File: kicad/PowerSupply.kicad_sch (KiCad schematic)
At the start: 10 parts, among them U3 LM2611xMF

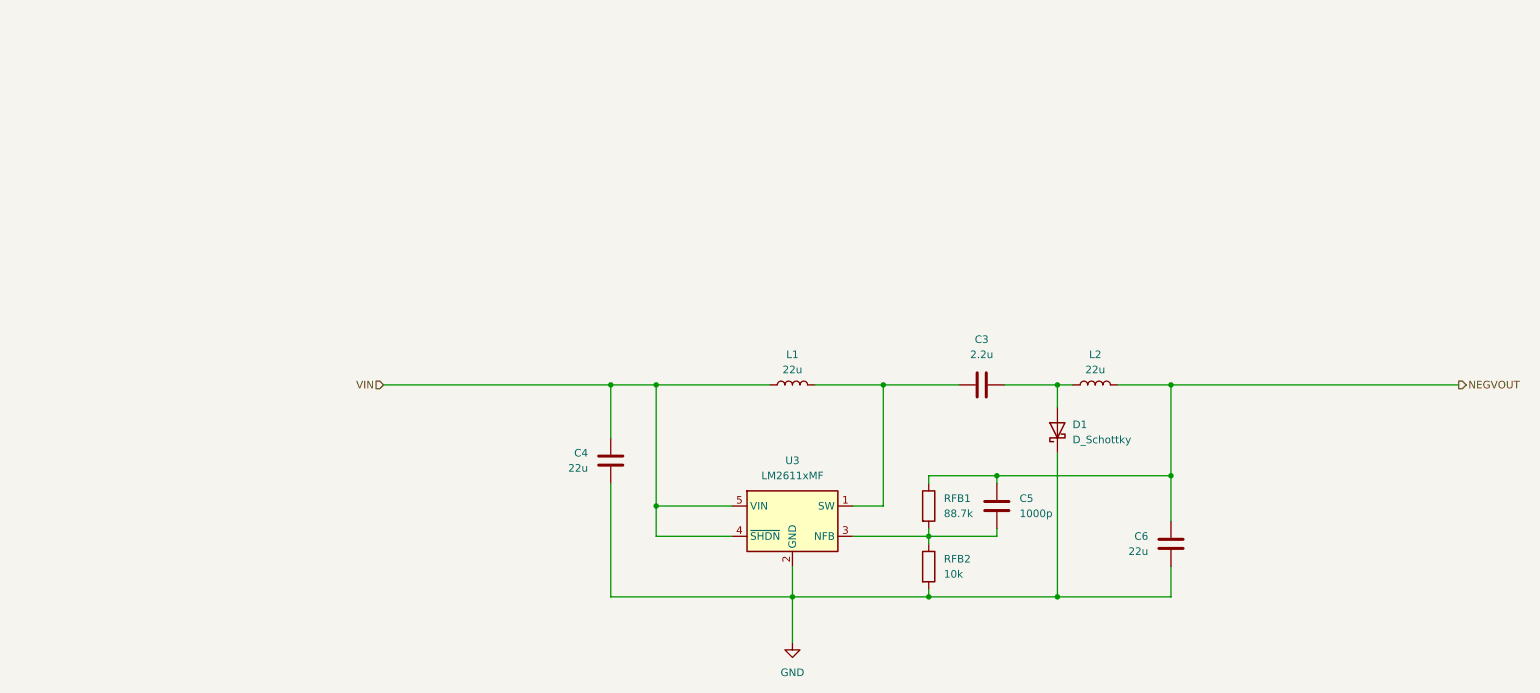
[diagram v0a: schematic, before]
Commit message: Refactored schematic into single page (except PSU)
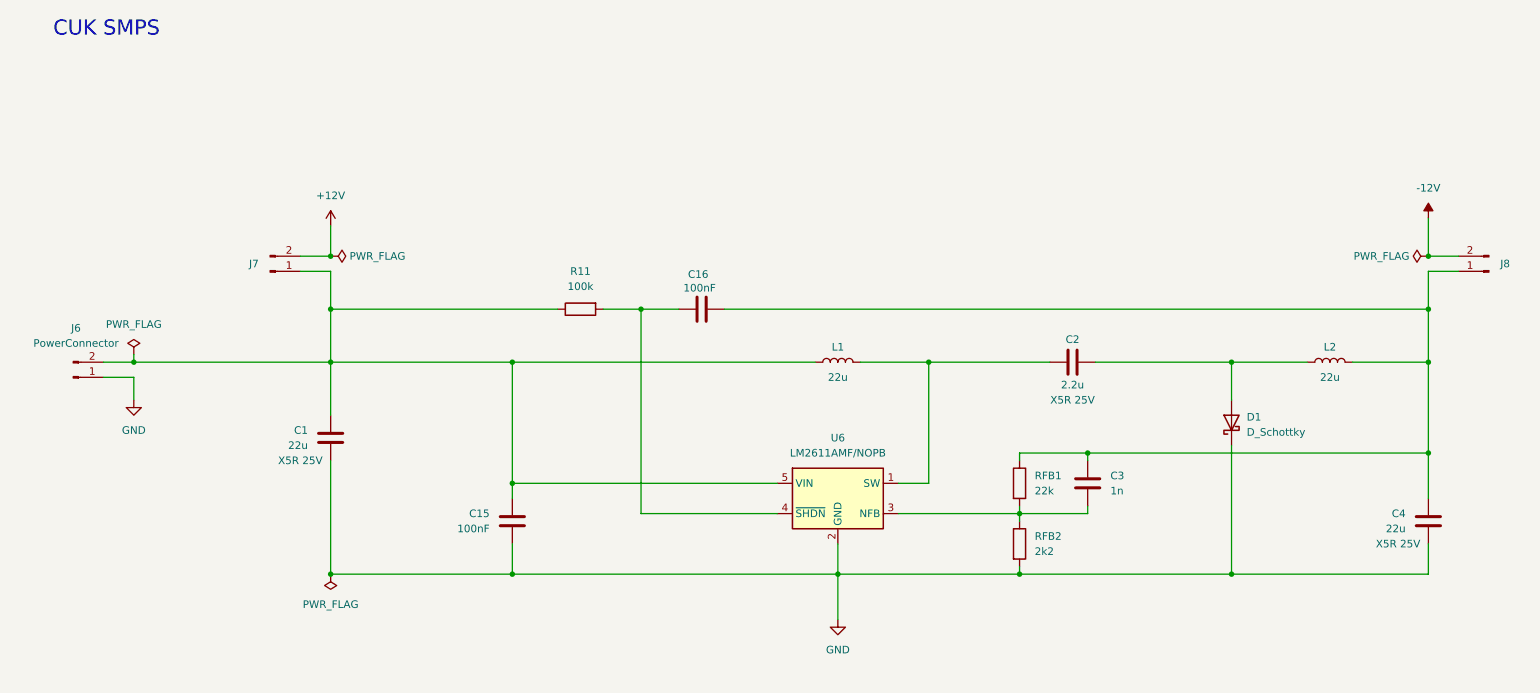
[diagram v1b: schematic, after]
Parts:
- removed C5: 1000p, symbol Device:C
- removed C6: 22u, symbol Device:C
- removed U3: LM2611xMF, Package_TO_SOT_SMD:SOT-23-5, symbol Regulator_Switching:LM2611xMF
- added C1: 22u, Capacitor_SMD:C_1210_3225Metric_Pad1.33x2.70mm_HandSolder, symbol Device:C
- added C15, C16: 100nF, Capacitor_SMD:C_0603_1608Metric_Pad1.08x0.95mm_HandSolder, symbol Device:C
- added C2: 2.2u, Capacitor_SMD:C_1210_3225Metric_Pad1.33x2.70mm_HandSolder, symbol Device:C
- added J6, J7, J8: PowerConnector, Connector_PinHeader_2.54mm:PinHeader_1x02_P2.54mm_Vertical, symbol Connector:Conn_01x02_Pin
- added R11: 100k, Resistor_SMD:R_0805_2012Metric_Pad1.20x1.40mm_HandSolder, symbol Device:R
- added U6: LM2611AMF/NOPB, Package_TO_SOT_SMD:SOT-23-5, symbol Regulator_Switching:LM2611xMF
- C3: value 2.2u -> 1n; footprint (none) -> Capacitor_SMD:C_0805_2012Metric_Pad1.18x1.45mm_HandSolder; LCSC (none) -> C15177; Mouser (none) -> 187-CL21B102JCANNNC; Notes (none) -> X7R 100V
- C4: footprint (none) -> Capacitor_SMD:C_1210_3225Metric_Pad1.33x2.70mm_HandSolder; LCSC (none) -> C52306; Mouser (none) -> 187-CL32A226KAJNNNE; Notes (none) -> X5R 25V
- D1: footprint (none) -> Diode_SMD:D_PowerDI-123; LCSC (none) -> C32150; Mouser (none) -> 863-MBRM120LT1G
- L1, L2: footprint (none) -> Inductor_SMD:L_Ferrocore_DLG-0403; LCSC (none) -> C2929420; Mouser (none) -> 815-ASPI-4020S-220MT; Notes (none) -> 270mΩ 600mA
- RFB1: value 88.7k -> 22k; footprint (none) -> Resistor_SMD:R_0805_2012Metric_Pad1.20x1.40mm_HandSolder; LCSC (none) -> C5121549; Mouser (none) -> 652-CR0805FX-8872ELF
- RFB2: value 10k -> 2k2; footprint (none) -> Resistor_SMD:R_0805_2012Metric_Pad1.20x1.40mm_HandSolder; LCSC (none) -> C17414; Mouser (none) -> 71-CRCW080510K0FKEAC
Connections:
- net GND: now also C1.1, C15.2, J6.1 (Pin_1), U6.2 (GND)
- net at D1.2 (A), L2.1: now also C2.2; no longer C3.2
- net at L1.2: now also C2.1, U6.1 (SW); no longer C3.1
- net at RFB1.2, RFB2.1: now also C3.1, U6.3 (NFB)
- net NEGVOUT: no longer names the net of L2.2, RFB1.1
- net NEGVOUT: now also C3.2, C4.2, C16.1, J8.1 (Pin_1)
- net VIN: no longer names the net of L1.1
- net VIN: now also C1.2, C15.1, J6.2 (Pin_2), J7.1 (Pin_1), R11.1, U6.5 (VIN); no longer C4.2
- new net: C16.2, R11.2, U6.4 (~{SHDN})
- new net +12V: J7.2 (Pin_2)
- new net -12V: J8.2 (Pin_2)
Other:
- note added: "CUK SMPS"

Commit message: - updated pots to rk12l12
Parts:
- J6: footprint Connector_PinHeader_2.54mm:PinHeader_1x02_P2.54mm_Vertical -> Connector_Molex:Molex_KK-254_AE-6410-02A_1x02_P2.54mm_Vertical
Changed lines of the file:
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@@
 			)
 		)
-		(property "Datasheet" "~"
+		(property "Datasheet" "https://www.mouser.co.uk/datasheet/2/3/ASPI-4020S-1775177.pdf"
 			(at 236.22 78.74 0)
 			(effects
@@
 			)
 		)
-		(property "Footprint" "Connector_PinHeader_2.54mm:PinHeader_1x02_P2.54mm_Vertical"
+		(property "Footprint" "Connector_Molex:Molex_KK-254_AE-6410-02A_1x02_P2.54mm_Vertical"
 			(at 25.4 81.28 0)
 			(effects
@@
 			)
 		)
-		(property "Datasheet" "~"
+		(property "Datasheet" "https://www.mouser.co.uk/datasheet/2/3/ASPI-4020S-1775177.pdf"
 			(at 153.67 78.74 0)
 			(effects

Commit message: replaced phono connectors with 3.5mm stereo jack connectors so that unplugged connections are switched to ground
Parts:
- R11, RFB1: LCSC C5121549 -> (none); Mouser 652-CR0805FX-8872ELF -> (none)
- RFB2: LCSC C17414 -> C1741; Mouser 71-CRCW080510K0FKEAC -> (none)
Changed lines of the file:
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@@
 			)
 		)
-		(property "LCSC" "C17414"
+		(property "LCSC" "C1741"
 			(at 184.15 109.22 0)
 			(effects
@@
 			)
 		)
-		(property "Mouser" "71-CRCW080510K0FKEAC"
+		(property "Mouser" ""
 			(at 184.15 109.22 0)
 			(effects
@@
 			)
 		)
-		(property "LCSC" "C5121549"
+		(property "LCSC" ""
 			(at 184.15 99.06 0)
 			(effects
@@
 			)
 		)
-		(property "Mouser" "652-CR0805FX-8872ELF"
+		(property "Mouser" ""
 			(at 184.15 99.06 0)
 			(effects
@@
 			)
 		)
-		(property "LCSC" "C5121549"
+		(property "LCSC" ""
 			(at 110.49 69.85 0)
 			(effects
@@
 			)
 		)
-		(property "Mouser" "652-CR0805FX-8872ELF"
+		(property "Mouser" ""
 			(at 110.49 69.85 0)
 			(effects
